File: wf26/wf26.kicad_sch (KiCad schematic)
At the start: 7 parts, among them J1 WF26 -> TV20 S bus

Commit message: Correct WF26 internal model; rework DESIGN.md; add TODO + schematic readout
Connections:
- net K1_COM: now also S1.1 (A); no longer S2.1 (A)
- net P1: now also LS1.1, WF26_K1.8 (coil); no longer C1.1, LS1.2
- net P2: now also S1.2 (B), S1.5 (B), S1.6 (C); no longer C1.2, R1.1, WF26_K1.5 (coil), WF26_K1.6 (NO)
- net P4: now also C1.2, R1.1, WF26_K1.5 (coil), WF26_K1.6 (NO); no longer S2.2 (B), S2.5 (B), S2.6 (C)
- net P5: now also C1.1, LS1.2; no longer LS1.1, WF26_K1.8 (coil)
- removed net OT_BRIDGE: R1.2, S1.2 (B), S1.5 (B)
- new net R1_BRIDGE: R1.2, S2.2 (B), S2.5 (B)
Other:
- note added: "5-wire bus toward TV20/S central unit: J1.1..5 = lines P1..P5 (P1-P4 direct bus conductors; line 5/P5 reaches the bus via the external Etagenruf button ET, not on this sheet)"
- note added: "P1 line 1 = common / reference (speech + ring return; LS1 & coil return)"
- note added: "P2 line 2 = listen down-audio + OeT door-opener pair; common of S1 (Tueroeffner)"
- note added: "P3 line 3 = talk up-audio + OeT door-opener pair; S2 (Sprechen) pressed ties P4-R1(2.2k)-P3"
- note added: "P4 line 4 = Tuerruf ring (~12V DC); C1/R1/coil/NO junction. Ring DC -> coil to P1; ring tone -> C1 -> LS1 (gong)"
- note added: "P5 line 5 = Etagenruf floor-call + speaker LS1 (+ C1) - reaches bus/TV20S via external ET button (Etagenruftaster, not on this sheet)"
- note added: "S1 (Tueroeffner) pressed: P2-P3 direct door-release bridge (no resistor). Released: P2-K1_COM."
- note added: "S2 (Sprechen) pressed = talk: P4-R1(2.2k)-P3. Coil P1-P4 (Tuerruf DC pulls K1 in); listen: P2 -> S1 released -> K1_COM -> NO -> P4 -> C1 -> LS1."
- note removed: "5-wire bus toward TV20/S central unit: J1.1..5 = lines P1..P5 (lines 1-4 are direct bus conductors; line 5/P5 reaches the bus via the external Etagenruf button ET, not on this sheet)"
- note removed: "P1 common / reference (speech + ring return)"
- note removed: "P2 listen leg - P4 reaches P2 via WF26_K1 NO only while a session energizes the coil; idle: NO open, P4 floats"
- note removed: "P3 talk leg - P4 ties here when the Sprechen button is pressed [measured: P3<->P4]"
- note removed: "P4 Tuerruf ring (~12V) + Sprechen/Hoeren PTT common (S2)"
- note removed: "P5 Etagenruf floor-call + speaker + relay-coil feed - reaches bus/TV20S via external ET button (Etagenruftaster, not on this sheet)"
- note removed: "S1 (OeT) pressed: P2-R1(2.2k)-P3 door-release bridge."
- note removed: "S2 PRESSED = talk: P4-P3. S2 RELEASED = idle/listen: P4-K1_COM->P2 via WF26_K1 NO (session active)."
- moved on the sheet: C1, LS1, R1, S1, S2, WF26_K1

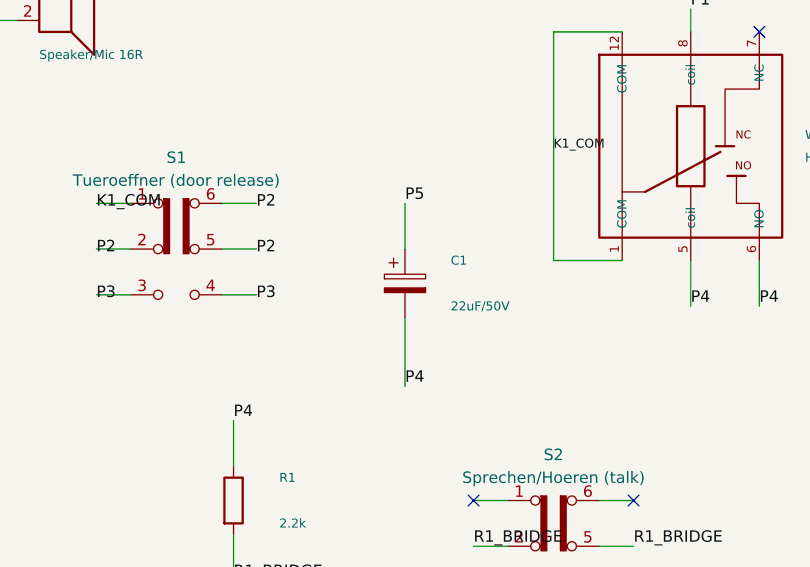
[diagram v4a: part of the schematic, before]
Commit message: WF26 core + enclosure fit: relay→SMD, cap polarity, switches, 59mm trim
- WF26_K1: THT HJR-4102 → SMD Omron G6K-2F-Y DC12 (Relay:G6K-2, LCSC
  C397194); rewired as SPDT — coil P1↔WF26_P4, COM(3)→NO(4) routes the
  listen path, spare pole no-connected
- WF26_C1: polarity flipped (+ → WF26_P4, the Türruf +12 V side)
- WF26_S1/S2: ALPS SPPJ223200 momentary DPDT symbol; pinout relabeled
  COM/NC/NO + mounting posts
- PCB: board trimmed to 64 × 59 mm for the WF26 enclosure (Edge.Cuts +
  zone outlines); components re-floorplanned/rotated; S1/S2 plunger
  reference crosshairs added on Dwgs.User
- Docs: C1 polarity corrected in DESIGN.md (+ → P4) and TODO; add
  docs/CBM5D33 (Sumida ESMIT-4180/C datasheet)
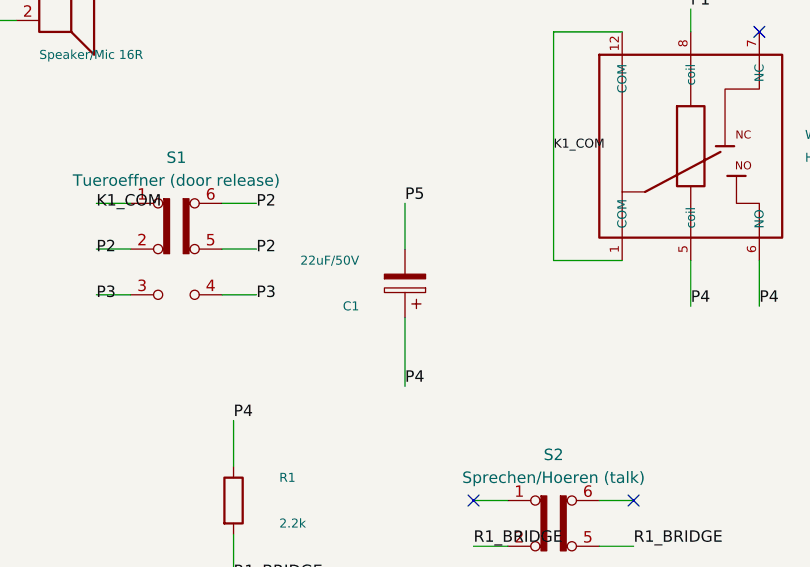
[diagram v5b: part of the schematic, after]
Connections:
- net P4: now also C1.1; no longer C1.2
- net P5: now also C1.2; no longer C1.1
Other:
- moved on the sheet: C1
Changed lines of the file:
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@@
 	(symbol
 		(lib_id "Device:C_Polarized")
-		(at 123.19 109.22 0)
+		(at 123.19 109.22 180)
 		(unit 1)
 		(body_style 1)
@@
 		(dnp no)
 		(property "Reference" "C1"
-			(at 128.27 106.68 0)
+			(at 118.11 111.76 0)
 			(show_name no)
 			(do_not_autoplace no)
@@
 		)
 		(property "Value" "22uF/50V"
-			(at 128.27 111.76 0)
+			(at 118.11 106.68 0)
 			(show_name no)
 			(do_not_autoplace no)
@@
 		)
 		(property "Datasheet" ""
-			(at 127 104.14 0)
+			(at 119.38 114.3 0)
 			(hide yes)
 			(show_name no)
@@
 		)
 		(property "Description" "Polarized capacitor"
-			(at 127 104.14 0)
+			(at 119.38 114.3 0)
 			(hide yes)
 			(show_name no)
